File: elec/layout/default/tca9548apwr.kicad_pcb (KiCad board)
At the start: 2 copper layers, 225.7 x 100.8 mm, 0 parts

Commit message: layout
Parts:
- added C1: Multilayer Ceramic Capacitors MLCC - SMD/SMT 100nF 10V 0402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, lib:C0402, F.Cu at (191.6, 52.3)
- added C2: Multilayer Ceramic Capacitors MLCC - SMD/SMT 2.2uF 10V 0603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, lib:C0603, F.Cu at (192.9, 52.3)
- added R1: Chip Resistor - Surface Mount 10KOhms ±5% 1/16W 0402 RoHS, lib:R0402, F.Cu at (195.7, 58.3)
- added R10: Chip Resistor - Surface Mount 10KOhms ±5% 1/16W 0402 RoHS, lib:R0402, F.Cu at (201.9, 45.9)
- added R11: Chip Resistor - Surface Mount 10KOhms ±5% 1/16W 0402 RoHS, lib:R0402, F.Cu at (198.8, 45.9)
- added R12: Chip Resistor - Surface Mount 10KOhms ±5% 1/16W 0402 RoHS, lib:R0402, F.Cu at (199.9, 45.9)
- added R13: Chip Resistor - Surface Mount 10KOhms ±5% 1/16W 0402 RoHS, lib:R0402, F.Cu at (196.7, 45.9)
- added R14: Chip Resistor - Surface Mount 10KOhms ±5% 1/16W 0402 RoHS, lib:R0402, F.Cu at (197.8, 45.9)
- added R15: Chip Resistor - Surface Mount 10KOhms ±5% 1/16W 0402 RoHS, lib:R0402, F.Cu at (194.6, 45.9)
- added R16: Chip Resistor - Surface Mount 10KOhms ±5% 1/16W 0402 RoHS, lib:R0402, F.Cu at (195.7, 45.9)
- added R2: Chip Resistor - Surface Mount 10KOhms ±5% 1/16W 0402 RoHS, lib:R0402, F.Cu at (194.6, 58.3)
- added R3: Chip Resistor - Surface Mount 10KOhms ±5% 1/16W 0402 RoHS, lib:R0402, F.Cu at (197.8, 58.3)
- added R4: Chip Resistor - Surface Mount 10KOhms ±5% 1/16W 0402 RoHS, lib:R0402, F.Cu at (196.7, 58.3)
- added R5: Chip Resistor - Surface Mount 10KOhms ±5% 1/16W 0402 RoHS, lib:R0402, F.Cu at (200.0, 58.3)
- added R6: Chip Resistor - Surface Mount 10KOhms ±5% 1/16W 0402 RoHS, lib:R0402, F.Cu at (198.9, 58.3)
- added R7: Chip Resistor - Surface Mount 10KOhms ±5% 1/16W 0402 RoHS, lib:R0402, F.Cu at (202.1, 58.3)
- added R8: Chip Resistor - Surface Mount 10KOhms ±5% 1/16W 0402 RoHS, lib:R0402, F.Cu at (201.0, 58.3)
- added R9: Chip Resistor - Surface Mount 10KOhms ±5% 1/16W 0402 RoHS, lib:R0402, F.Cu at (200.9, 45.9)
- added U1: , lib:TSSOP-24_L7.8-W4.4-P0.65-LS6.4-BL, F.Cu at (198.0, 52.2)
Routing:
- net gnd: track 0.00 -> 4.80 mm
- net vcc: track 0.00 -> 4.48 mm
- net scl-7: track 0.00 -> 4.21 mm
- net sda-7: track 0.00 -> 3.89 mm
- net sda: track 0.00 -> 3.51 mm
- net scl-3: track 0.00 -> 3.42 mm
- net scl-6: track 0.00 -> 3.40 mm
- net sda-6: track 0.00 -> 3.24 mm
- net scl: track 0.00 -> 3.13 mm
- net scl-5: track 0.00 -> 3.07 mm
- net sda-1: track 0.00 -> 2.99 mm
- net sda-3: track 0.00 -> 2.94 mm
- net sda-5: track 0.00 -> 2.91 mm
- net sda-4: track 0.00 -> 2.89 mm
- net scl-1: track 0.00 -> 2.84 mm
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
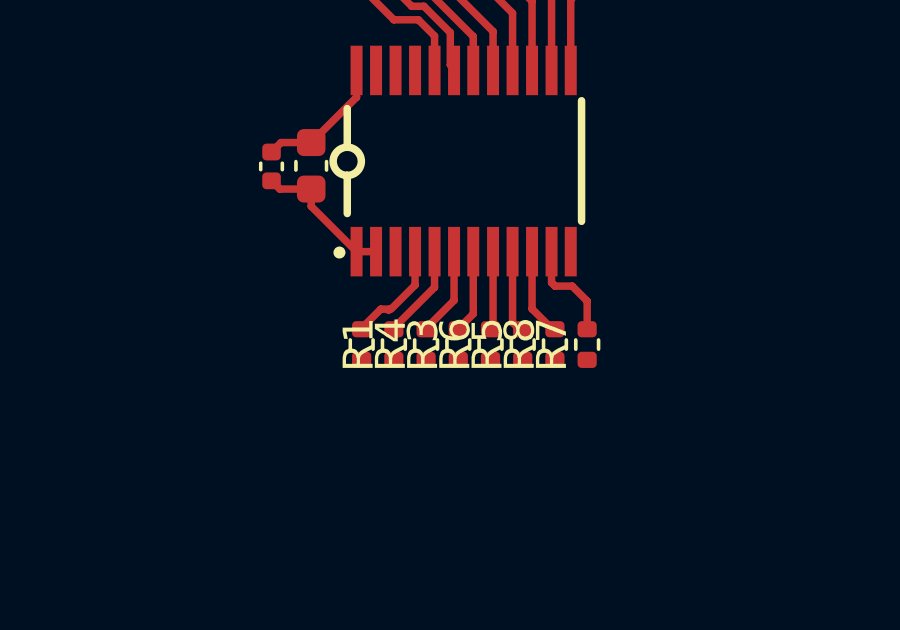
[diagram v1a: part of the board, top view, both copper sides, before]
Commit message: Add reset resistor to layout
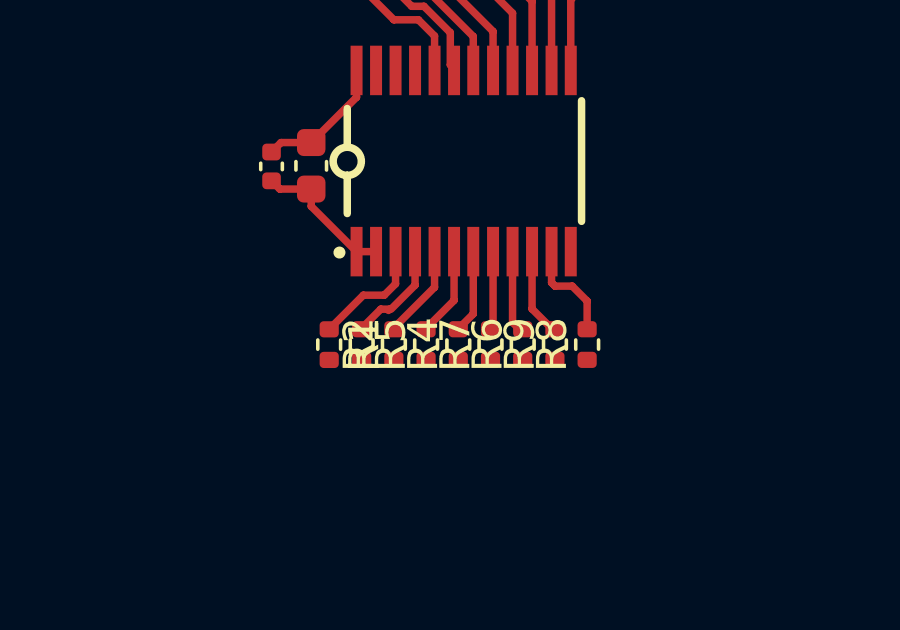
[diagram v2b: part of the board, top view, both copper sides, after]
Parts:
- added R1: 62.5mW Thick Film Resistors 50V ±100ppm/℃ ±1% 10kΩ 0402 Chi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, lib:R0402, F.Cu at (193.5, 58.3)
- C1: value Multilayer Ceramic Capacitors MLCC - SMD/SMT 100nF 10V 0402 RoHS -> 16V 100nF X7R ±10% 0402 Multilayer Ceramic Capacitors MLCC - SMD/SMT ROHS
- C2: value Multilayer Ceramic Capacitors MLCC - SMD/SMT 2.2uF 10V 0603 RoHS -> 16V 2.2uF X5R ±10% 0603 Multilayer Ceramic Capacitors MLCC - SMD/SMT ROHS
- R10: renamed from R9; value Chip Resistor - Surface Mount 10KOhms ±5% 1/16W 0402 RoHS -> 62.5mW Thick Film Resistors 50V ±100ppm/℃ ±1% 10kΩ 0402 Chip Resistor - Surface Mount ROHS
- R11: renamed from R10; value Chip Resistor - Surface Mount 10KOhms ±5% 1/16W 0402 RoHS -> 62.5mW Thick Film Resistors 50V ±100ppm/℃ ±1% 10kΩ 0402 Chip Resistor - Surface Mount ROHS
- R12: renamed from R11; value Chip Resistor - Surface Mount 10KOhms ±5% 1/16W 0402 RoHS -> 62.5mW Thick Film Resistors 50V ±100ppm/℃ ±1% 10kΩ 0402 Chip Resistor - Surface Mount ROHS
- R13: renamed from R12; value Chip Resistor - Surface Mount 10KOhms ±5% 1/16W 0402 RoHS -> 62.5mW Thick Film Resistors 50V ±100ppm/℃ ±1% 10kΩ 0402 Chip Resistor - Surface Mount ROHS
- R14: renamed from R13; value Chip Resistor - Surface Mount 10KOhms ±5% 1/16W 0402 RoHS -> 62.5mW Thick Film Resistors 50V ±100ppm/℃ ±1% 10kΩ 0402 Chip Resistor - Surface Mount ROHS
- R15: renamed from R14; value Chip Resistor - Surface Mount 10KOhms ±5% 1/16W 0402 RoHS -> 62.5mW Thick Film Resistors 50V ±100ppm/℃ ±1% 10kΩ 0402 Chip Resistor - Surface Mount ROHS
- R16: renamed from R15; value Chip Resistor - Surface Mount 10KOhms ±5% 1/16W 0402 RoHS -> 62.5mW Thick Film Resistors 50V ±100ppm/℃ ±1% 10kΩ 0402 Chip Resistor - Surface Mount ROHS
- R17: renamed from R16; value Chip Resistor - Surface Mount 10KOhms ±5% 1/16W 0402 RoHS -> 62.5mW Thick Film Resistors 50V ±100ppm/℃ ±1% 10kΩ 0402 Chip Resistor - Surface Mount ROHS
- R2: renamed from R1; value Chip Resistor - Surface Mount 10KOhms ±5% 1/16W 0402 RoHS -> 62.5mW Thick Film Resistors 50V ±100ppm/℃ ±1% 10kΩ 0402 Chip Resistor - Surface Mount ROHS
- R3: renamed from R2; value Chip Resistor - Surface Mount 10KOhms ±5% 1/16W 0402 RoHS -> 62.5mW Thick Film Resistors 50V ±100ppm/℃ ±1% 10kΩ 0402 Chip Resistor - Surface Mount ROHS
- R4: renamed from R3; value Chip Resistor - Surface Mount 10KOhms ±5% 1/16W 0402 RoHS -> 62.5mW Thick Film Resistors 50V ±100ppm/℃ ±1% 10kΩ 0402 Chip Resistor - Surface Mount ROHS
- R5: renamed from R4; value Chip Resistor - Surface Mount 10KOhms ±5% 1/16W 0402 RoHS -> 62.5mW Thick Film Resistors 50V ±100ppm/℃ ±1% 10kΩ 0402 Chip Resistor - Surface Mount ROHS
- R6: renamed from R5; value Chip Resistor - Surface Mount 10KOhms ±5% 1/16W 0402 RoHS -> 62.5mW Thick Film Resistors 50V ±100ppm/℃ ±1% 10kΩ 0402 Chip Resistor - Surface Mount ROHS
- R7: renamed from R6; value Chip Resistor - Surface Mount 10KOhms ±5% 1/16W 0402 RoHS -> 62.5mW Thick Film Resistors 50V ±100ppm/℃ ±1% 10kΩ 0402 Chip Resistor - Surface Mount ROHS
- R8: renamed from R7; value Chip Resistor - Surface Mount 10KOhms ±5% 1/16W 0402 RoHS -> 62.5mW Thick Film Resistors 50V ±100ppm/℃ ±1% 10kΩ 0402 Chip Resistor - Surface Mount ROHS
- R9: renamed from R8; value Chip Resistor - Surface Mount 10KOhms ±5% 1/16W 0402 RoHS -> 62.5mW Thick Film Resistors 50V ±100ppm/℃ ±1% 10kΩ 0402 Chip Resistor - Surface Mount ROHS
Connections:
- net gnd renamed ic-gnd
- net scl renamed ic-scl
- net scl-1 renamed ic-scl-1
- net scl-2 renamed ic-scl-2
- net scl-3 renamed ic-scl-3
- net scl-4 renamed ic-scl-4
- net scl-5 renamed ic-scl-5
- net scl-6 renamed ic-scl-6
- net scl-7 renamed ic-scl-7
- net scl-8 renamed ic-scl-8
- net sda renamed ic-sda
- net sda-1 renamed ic-sda-1
- net sda-2 renamed ic-sda-2
- net sda-3 renamed ic-sda-3
- net sda-4 renamed ic-sda-4
- net sda-5 renamed ic-sda-5
- net sda-6 renamed ic-sda-6
- net sda-7 renamed ic-sda-7
- net sda-8 renamed ic-sda-8
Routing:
- net reset_: track 0.00 -> 3.91 mm

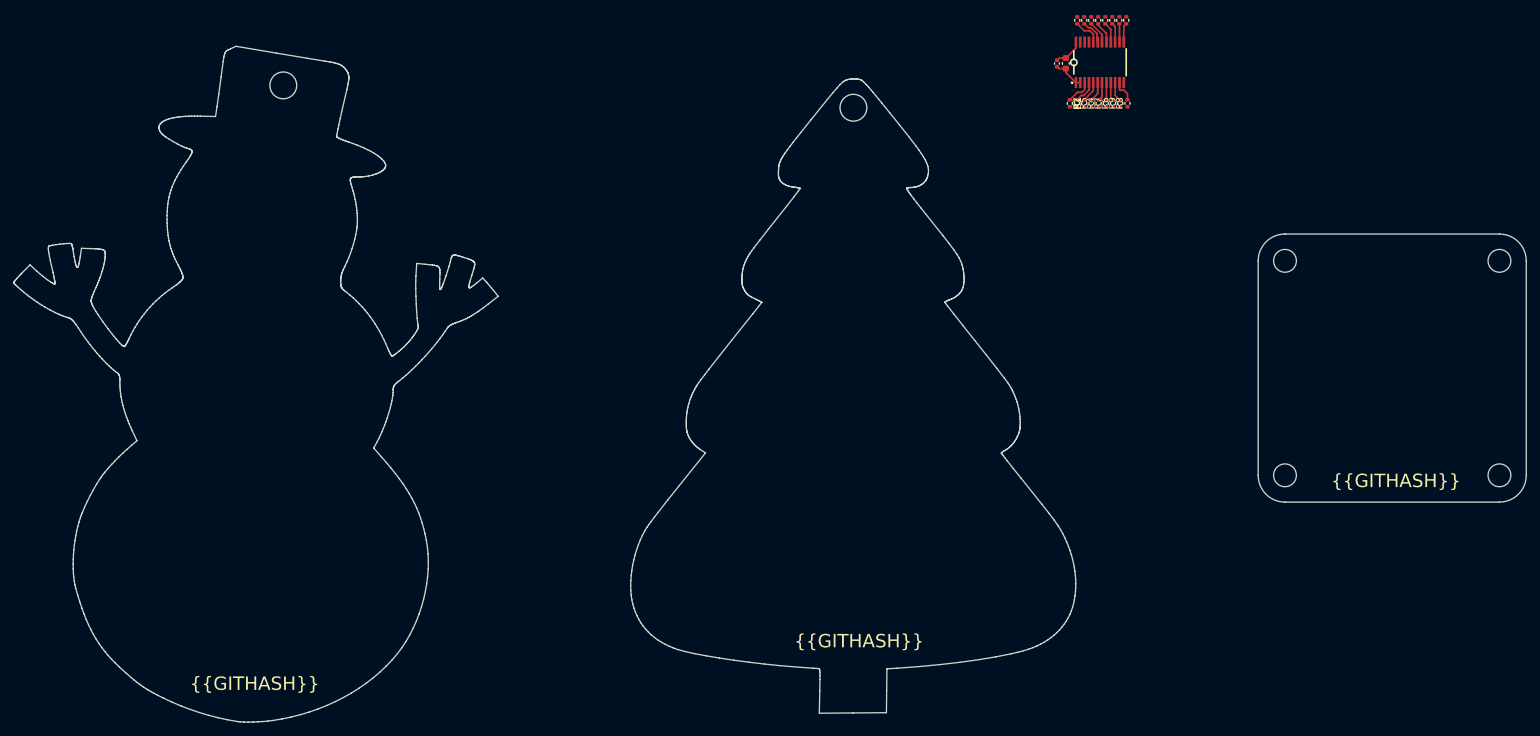
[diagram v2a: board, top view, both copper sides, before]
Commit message: Remove xmas characters from layout
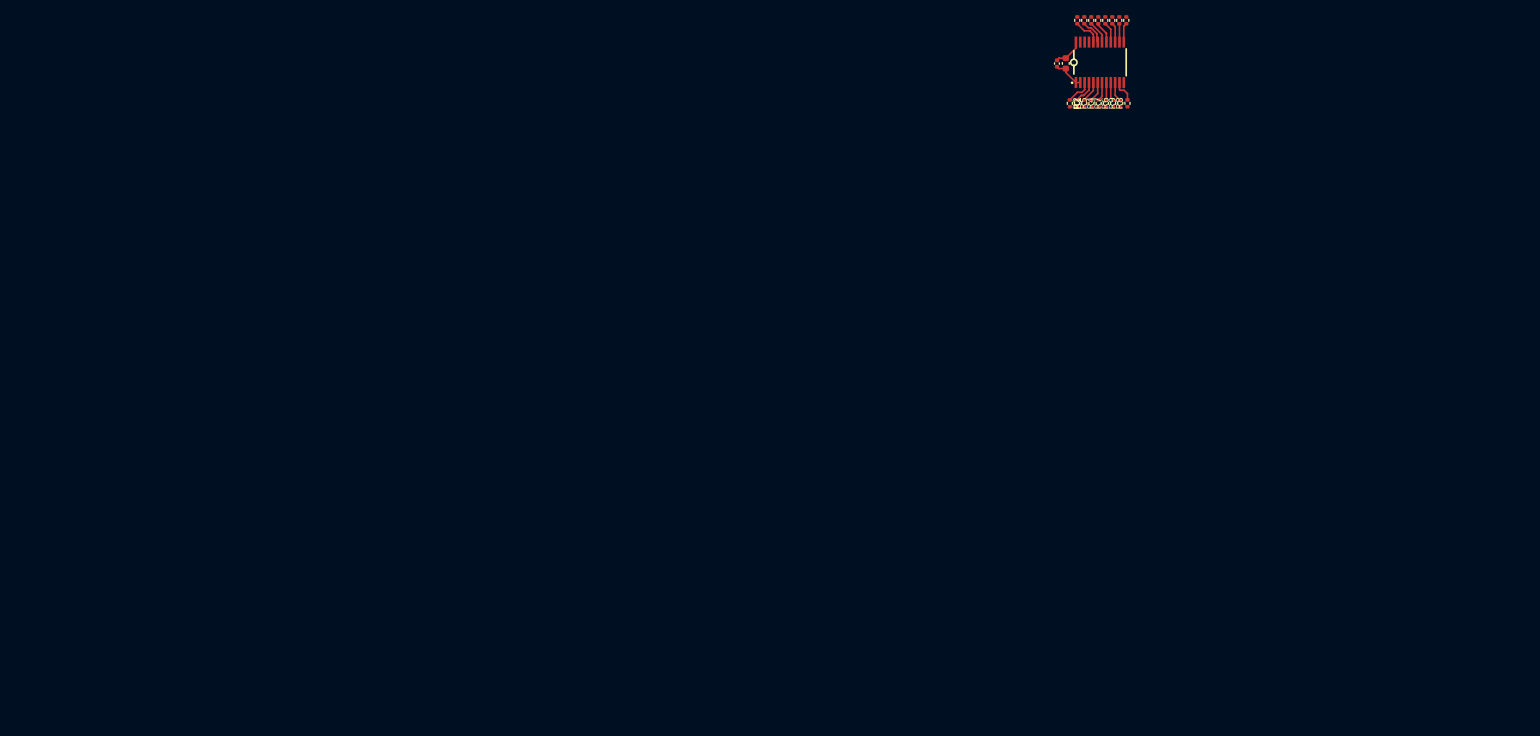
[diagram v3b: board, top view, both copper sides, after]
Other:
- board outline removed
- board text removed: "{{GITHASH}}"

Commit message: run build, update layout
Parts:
- C1: value 16V 100nF X7R ±10% 0402 Multilayer Ceramic Capacitors MLCC - SMD/SMT ROHS -> 100nF ±10% 16V X7R; footprint lib:C0402 -> lcsc:C0402
- C2: value 16V 2.2uF X5R ±10% 0603 Multilayer Ceramic Capacitors MLCC - SMD/SMT ROHS -> 2.2µF ±10% 25V X5R; footprint lib:C0603 -> lcsc:C0603
- R1, R10, R11, R12, R13, R14, R15, R16, R17, R2, R3, R4, R5, R6, R7, R8, R9: value 62.5mW Thick Film Resistors 50V ±100ppm/℃ ±1% 10kΩ 0402 Chip Resistor - Surface Mount ROHS -> 10kΩ ±1% 62.5mW; footprint lib:R0402 -> lcsc:R0402
- U1: value (none) -> _TCA9548APWR
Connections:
- net ic-gnd renamed gnd
- net ic-scl renamed scl-5
- net ic-scl-1 renamed scl
- net ic-scl-2 renamed scl-2
- net ic-scl-3 renamed scl-6
- net ic-scl-4 renamed scl-3
- net ic-scl-5 renamed scl-4
- net ic-scl-6 renamed scl-7
- net ic-scl-7 renamed scl-1
- net ic-scl-8 renamed SCL
- net ic-sda renamed sda-5
- net ic-sda-1 renamed sda-7
- net ic-sda-2 renamed sda-3
- net ic-sda-3 renamed sda-6
- net ic-sda-4 renamed sda-4
- net ic-sda-5 renamed sda
- net ic-sda-6 renamed sda-2
- net ic-sda-7 renamed sda-1
- net ic-sda-8 renamed SDA
- net reset_ renamed io
- net vcc renamed hv

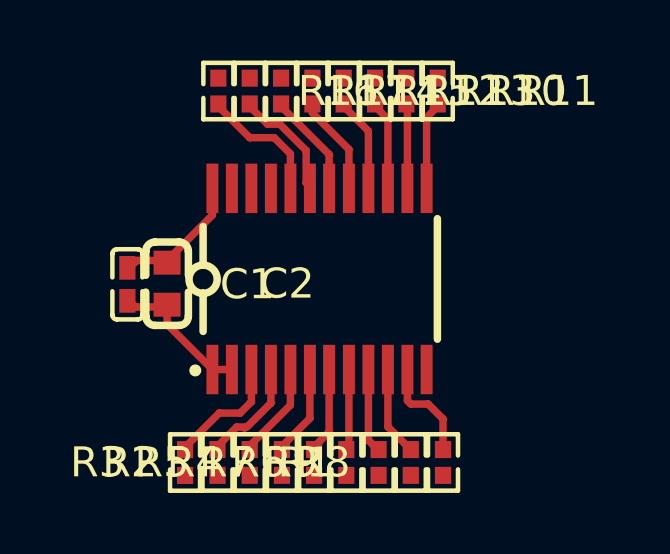
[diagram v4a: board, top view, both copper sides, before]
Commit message: update syntax and link layout
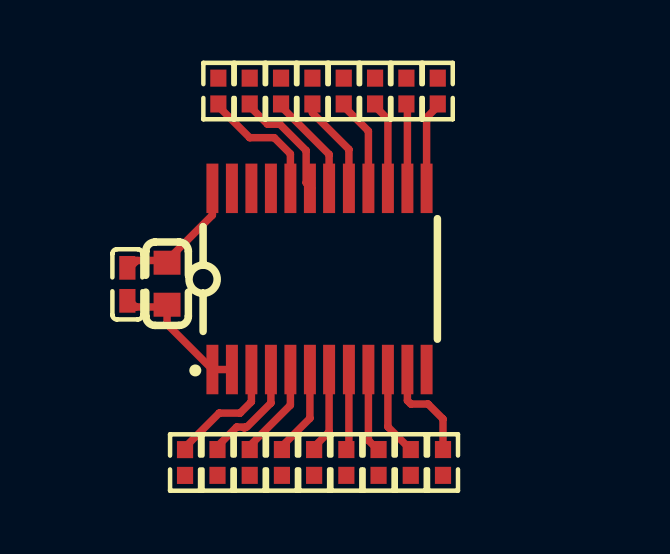
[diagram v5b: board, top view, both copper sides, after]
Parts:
- C1: footprint lcsc:C0402 -> atopile:C0402-b3ef17
- C2: value 2.2µF ±10% 25V X5R -> 2.2µF ±10% 16V X5R; footprint lcsc:C0603 -> atopile:C0603-bd72f6
- R1, R10, R11, R12, R13, R14, R15, R16, R17, R2, R3, R4, R5, R6, R7, R8, R9: footprint lcsc:R0402 -> atopile:R0402-56259e
- U1: value _TCA9548APWR -> (none)
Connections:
- net io renamed RESET_
- net scl renamed line-12
- net scl-1 renamed line-9
- net scl-2 renamed line-3
- net scl-3 renamed line-1
- net scl-4 renamed line-5
- net scl-5 renamed line
- net scl-6 renamed line-6
- net scl-7 renamed line-14
- net sda renamed line-7
- net sda-1 renamed line-8
- net sda-2 renamed line-10
- net sda-3 renamed line-11
- net sda-4 renamed line-13
- net sda-5 renamed line-15
- net sda-6 renamed line-2
- net sda-7 renamed line-4

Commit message: Fix frozen
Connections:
- R1 pad 1: RESET_ -> line-13
- R10 pad 1: hv -> line-10
- R10 pad 2: line-1 -> hv
- R11 pad 1: hv -> line-8
- R11 pad 2: line-13 -> hv
- R12 pad 1: hv -> line
- R12 pad 2: line-5 -> hv
- R13 pad 1: hv -> line-16
- R13 pad 2: line-7 -> hv
- R14 pad 1: hv -> line-2
- R14 pad 2: line-14 -> hv
- R15 pad 1: hv -> line-3
- R15 pad 2: line-10 -> hv
- R16 pad 1: hv -> line-5
- R16 pad 2: line-9 -> hv
- R17 pad 1: hv -> line-15
- R17 pad 2: line-8 -> hv
- R2 pad 1: hv -> line-14
- R2 pad 2: line -> hv
- R3 pad 1: hv -> line-4
- R3 pad 2: line-15 -> hv
- R4 pad 1: hv -> line-12
- R4 pad 2: line-12 -> hv
- R5 pad 1: hv -> line-1
- R5 pad 2: line-4 -> hv
- R6 pad 1: hv -> line-9
- R6 pad 2: line-3 -> hv
- R7 pad 1: hv -> line-7
- R7 pad 2: line-11 -> hv
- R8 pad 1: hv -> line-11
- R8 pad 2: line-6 -> hv
- R9 pad 1: hv -> line-6
- R9 pad 2: line-2 -> hv
- U1 pad 10: line-2 -> line-6
- U1 pad 11: line-6 -> line-11
- U1 pad 13: line-13 -> line-8
- U1 pad 14: line-1 -> line-10
- U1 pad 15: line-7 -> line-16
- U1 pad 16: line-5 -> line
- U1 pad 17: line-10 -> line-3
- U1 pad 18: line-14 -> line-2
- U1 pad 19: line-8 -> line-15
- U1 pad 20: line-9 -> line-5
- U1 pad 3: RESET_ -> line-13
- U1 pad 4: line-15 -> line-4
- U1 pad 5: line -> line-14
- U1 pad 6: line-4 -> line-1
- U1 pad 8: line-11 -> line-7
- U1 pad 9: line-3 -> line-9
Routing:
- net (no net): track 0.00 -> 31.6 mm
- net line-9: track 4.21 -> 0.00 mm
- net line-13: track 2.89 -> 6.80 mm
- net RESET_: track 3.91 -> 0.00 mm
- net line-15: track 3.51 -> 0.00 mm
- net line-6: track 3.42 -> 0.00 mm
- net line-14: track 3.40 -> 0.00 mm
- net line-4: track 2.99 -> 0.00 mm
- net line-2: track 2.94 -> 0.00 mm
- net line-7: track 2.91 -> 0.00 mm
- net line-3: track 2.78 -> 0.00 mm
- net line-1: track 2.75 -> 0.00 mm
- net line-11: track 2.70 -> 0.00 mm

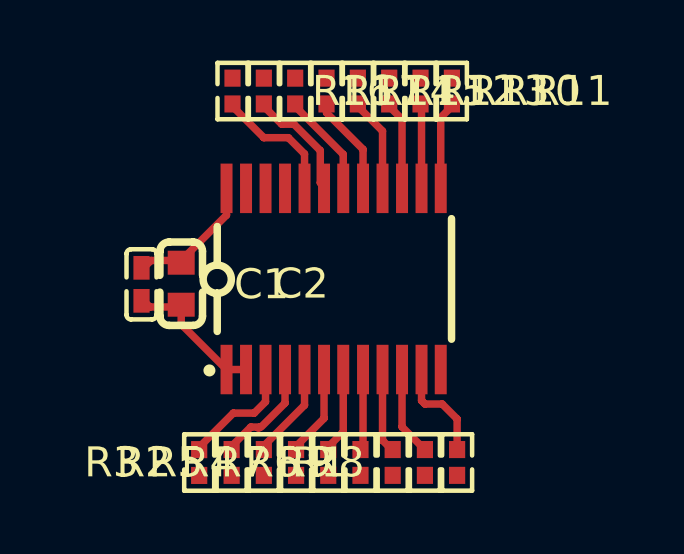
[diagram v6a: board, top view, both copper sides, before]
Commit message: update to kicad 9 and fix resistor orientation
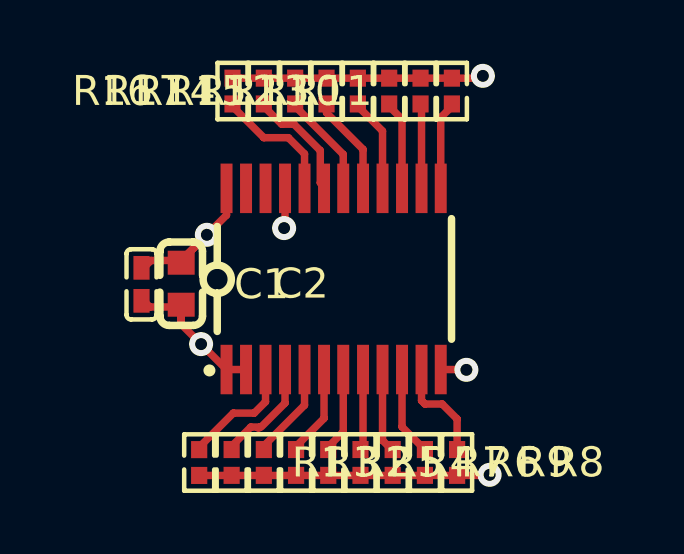
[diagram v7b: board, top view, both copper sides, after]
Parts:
- turned R10 to 90 degrees
- turned R11 to 90 degrees
- turned R12 to 90 degrees
- turned R13 to 90 degrees
- turned R14 to 90 degrees
- turned R15 to 90 degrees
- turned R16 to 90 degrees
- turned R17 to 90 degrees
- turned R2 to -90 degrees
- turned R3 to -90 degrees
- turned R4 to -90 degrees
- turned R5 to -90 degrees
- turned R6 to -90 degrees
- turned R7 to -90 degrees
- turned R8 to -90 degrees
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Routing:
- net (no net): track 31.6 -> 0.00 mm
- net hv: track 4.48 -> 23.8 mm, vias 0 -> 3
- net line-15: track 0.00 -> 3.89 mm
- net line-4: track 0.00 -> 3.51 mm
- net line-11: track 0.00 -> 3.42 mm
- net line-2: track 0.00 -> 3.40 mm
- net line-3: track 0.00 -> 3.24 mm
- net line-14: track 0.00 -> 3.13 mm
- net line-1: track 0.00 -> 2.99 mm
- net line-6: track 0.00 -> 2.94 mm
- net line-16: track 0.00 -> 2.91 mm
- net line-13: track 6.80 -> 3.91 mm
- net gnd: track 4.80 -> 7.64 mm, vias 0 -> 3
- net line-9: track 0.00 -> 2.78 mm
- net line-7: track 0.00 -> 2.70 mm
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
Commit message: build with latest
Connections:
- net line renamed SC5
- net line-1 renamed SD1
- net line-10 renamed SC4
- net line-11 renamed SC3
- net line-12 renamed SC1
- net line-13 renamed RESET_
- net line-14 renamed SC0
- net line-15 renamed SD7
- net line-16 renamed SD5
- net line-2 renamed SC6
- net line-3 renamed SD6
- net line-4 renamed SD0
- net line-5 renamed SC7
- net line-6 renamed SD3
- net line-7 renamed SD2
- net line-8 renamed SD4
- net line-9 renamed SC2
